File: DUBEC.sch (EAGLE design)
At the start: 47 parts

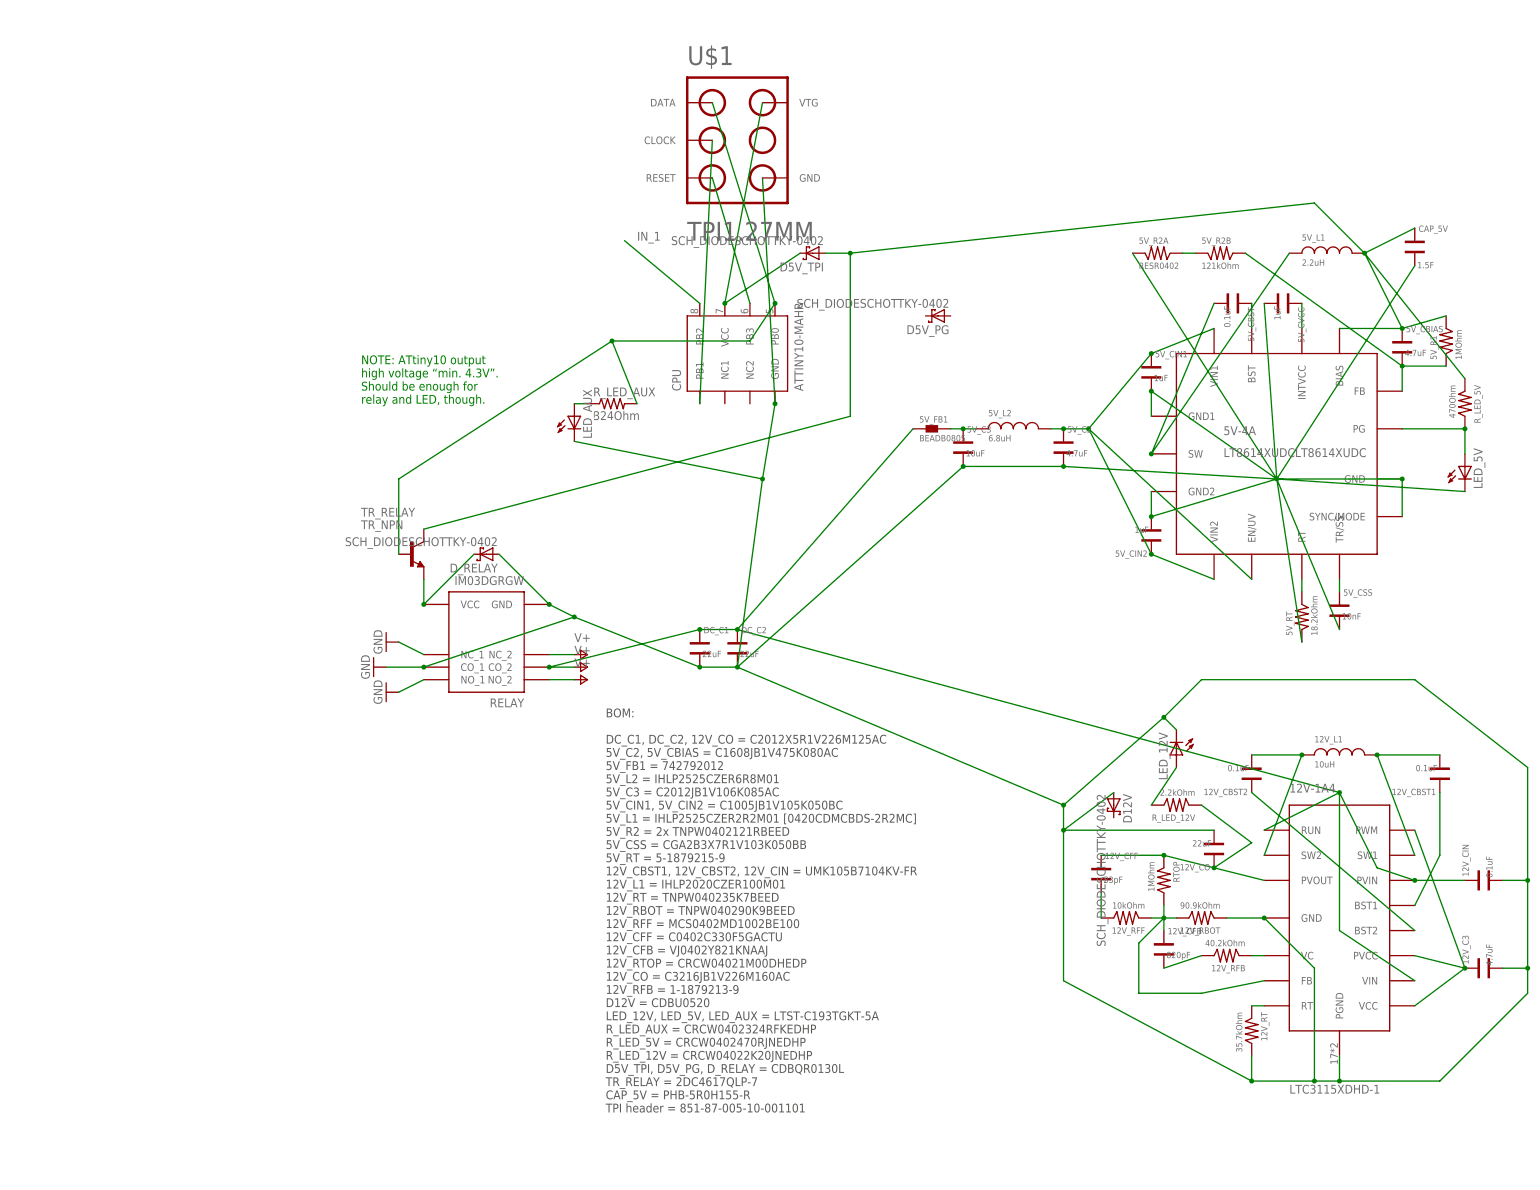
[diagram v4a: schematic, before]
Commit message: Switch to ATtiny13A (EEPROM)
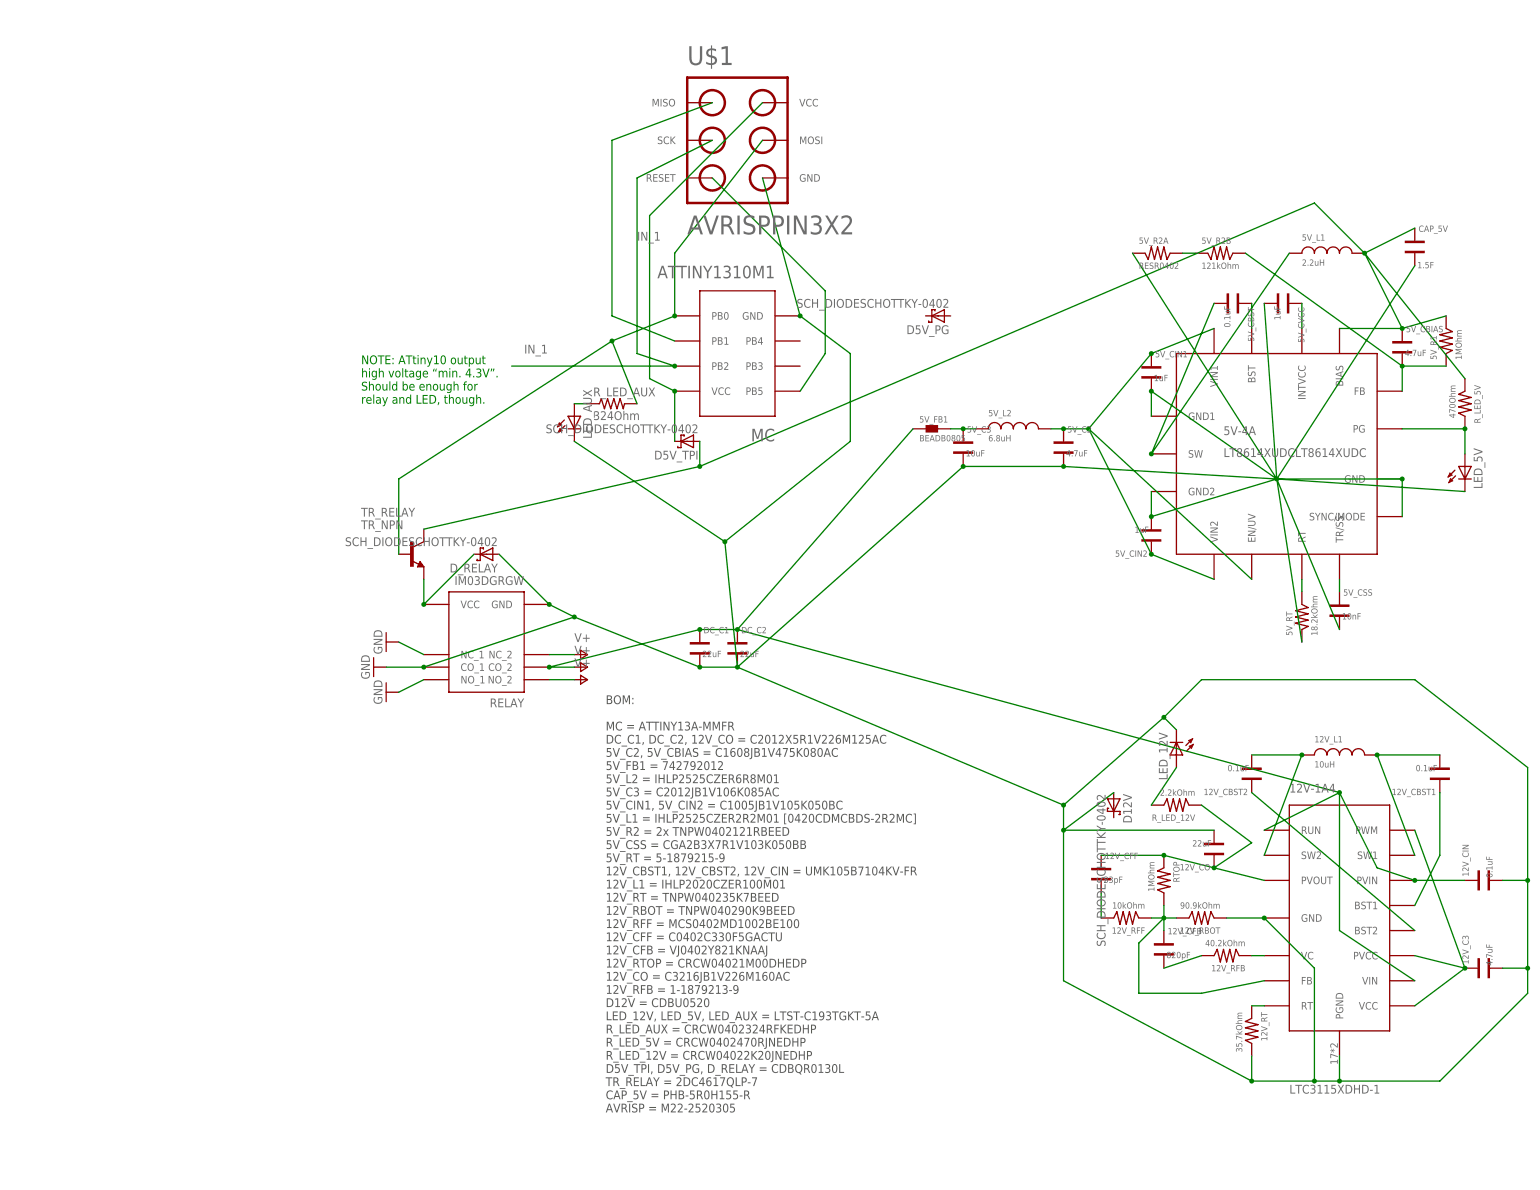
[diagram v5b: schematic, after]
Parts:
- removed CPU: ATTINY10-MAHR, jne:ATTINY10-MAHR
- added MC: ATTINY1310M1, dubec:ATTINY1310M1
- U$1: value TPI1.27MM -> AVRISPPIN3X2; device dubec:TPI1.27MM -> dubec:AVRISPPIN3X2
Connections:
- removed net 5V_TPI: CPU.VCC, D5V_TPI.C, U$1.VTG
- removed net PB1: CPU.PB1, U$1.CLOCK
- removed net PB3: CPU.PB3, U$1.RESET
- new net 5V_ISP: D5V_TPI.C, MC.VCC, U$1.VCC
- new net N$11: MC.PB5, U$1.RESET
- new net N$16: MC.PB1, U$1.MISO
- net GND: now also MC.GND; no longer CPU.GND
- net IN_1: now also MC.PB2, U$1.SCK; no longer CPU.PB2
- net PB0: now also MC.PB0, U$1.MOSI; no longer CPU.PB0, U$1.DATA
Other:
- note added: "BOM: MC = ATTINY13A-MMFR DC_C1, DC_C2, 12V_CO = C2012X5R1V226M125AC 5V_C2, 5V_CBIAS = C1608JB1V475K080AC 5V_FB1 = 742792012 5V_L2 = IHLP2525CZER6R8M01 5V_C3 = C2012JB1V106K085AC 5V_CIN1, 5V_CIN2 = C1005JB1V105K050BC 5V_L1 = IHLP2525CZER2R2M01 [0420CDMCBDS-2R2MC] 5V_R2 = 2x TNPW0402121RBEED 5V_CSS = CGA2B3X7R1V103K050BB 5V_RT = 5-1879215-9 12V_CBST1, 12V_CBST2, 12V_CIN = UMK105B7104KV-FR 12V_L1 = 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"
- note removed: "BOM: DC_C1, DC_C2, 12V_CO = C2012X5R1V226M125AC 5V_C2, 5V_CBIAS = C1608JB1V475K080AC 5V_FB1 = 742792012 5V_L2 = IHLP2525CZER6R8M01 5V_C3 = C2012JB1V106K085AC 5V_CIN1, 5V_CIN2 = C1005JB1V105K050BC 5V_L1 = IHLP2525CZER2R2M01 [0420CDMCBDS-2R2MC] 5V_R2 = 2x TNPW0402121RBEED 5V_CSS = CGA2B3X7R1V103K050BB 5V_RT = 5-1879215-9 12V_CBST1, 12V_CBST2, 12V_CIN = UMK105B7104KV-FR 12V_L1 = IHLP2020CZER100M01 1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"
- moved on the sheet: D5V_TPI
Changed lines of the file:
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@@
 <parts>
 <part name="5V-4A" library="jne" deviceset="LT8614XUDC" device="LT8614XUDC"/>
-<part name="CPU" library="jne" deviceset="ATTINY10-MAHR" device=""/>
+<part name="MC" library="dubec" deviceset="ATTINY13" device="10M1"/>
 <part name="RELAY" library="jne" deviceset="IM03DGR" device="GW"/>
 <part name="12V-1A4" library="jne" deviceset="LTC3115XDHD-1" device=""/>
@@
 <part name="R_LED_12V" library="jne" deviceset="RES" device="R0402" value="2.2kOhm"/>
 <part name="R_LED_5V" library="jne" deviceset="RES" device="R0402" value="470Ohm"/>
-<part name="U$1" library="dubec" deviceset="TPI" device="1.27MM" value="TPI1.27MM"/>
+<part name="U$1" library="dubec" deviceset="AVRISP" device="PIN3X2" value="AVRISPPIN3X2"/>
 <part name="D5V_PG" library="dubec" deviceset="SCH_DIODE" device="SCHOTTKY-0402"/>
 <part name="D5V_TPI" library="dubec" deviceset="SCH_DIODE" device="SCHOTTKY-0402"/>
@@
 <plain>
 <text x="-67.31" y="-107.95" size="1.778" layer="97">BOM:
+MC = ATTINY13A-MMFR
 DC_C1, DC_C2, 12V_CO = C2012X5R1V226M125AC
 5V_C2, 5V_CBIAS = C1608JB1V475K080AC
@@
 TR_RELAY = 2DC4617QLP-7
 CAP_5V = PHB-5R0H155-R
-TPI header = 851-87-005-10-001101
+AVRISP = M22-2520305
 </text>
 <text x="-116.84" y="35.56" size="1.778" layer="91">NOTE: ATtiny10 output
@@
 <instances>
 <instance part="5V-4A" gate="G$1" x="68.58" y="25.4"/>
-<instance part="CPU" gate="G$1" x="-40.64" y="45.72" rot="R90"/>
+<instance part="MC" gate="G$1" x="-40.64" y="45.72" rot="R180"/>
 <instance part="RELAY" gate="G$1" x="-91.44" y="-12.7" rot="R180"/>
 <instance part="12V-1A4" gate="G$1" x="81.28" y="-68.58"/>
@@
 <instance part="U$1" gate="G$1" x="-40.64" y="88.9"/>
 <instance part="D5V_PG" gate="G$1" x="0" y="53.34" rot="R180"/>
-<instance part="D5V_TPI" gate="G$1" x="-25.4" y="66.04" rot="R180"/>
+<instance part="D5V_TPI" gate="G$1" x="-50.8" y="27.94" rot="R180"/>
 <instance part="TR_RELAY" gate="G$1" x="-106.68" y="5.08"/>
 <instance part="D_RELAY" gate="G$1" x="-91.44" y="5.08" rot="R180"/>
@@
 <wire x1="106.68" y1="40.64" x2="86.36" y2="66.04" width="0.1524" layer="91"/>
 <pinref part="D5V_TPI" gate="G$1" pin="A"/>
-<wire x1="-22.86" y1="66.04" x2="-17.78" y2="66.04" width="0.1524" layer="91"/>
-<wire x1="-17.78" y1="66.04" x2="76.2" y2="76.2" width="0.1524" layer="91"/>
+<wire x1="-48.26" y1="27.94" x2="-48.26" y2="22.86" width="0.1524" layer="91"/>
+<wire x1="-48.26" y1="22.86" x2="76.2" y2="76.2" width="0.1524" layer="91"/>
 <wire x1="76.2" y1="76.2" x2="86.36" y2="66.04" width="0.1524" layer="91"/>
-<wire x1="-17.78" y1="66.04" x2="-17.78" y2="33.02" width="0.1524" layer="91"/>
-<junction x="-17.78" y="66.04"/>
+<junction x="-48.26" y="22.86"/>
 <pinref part="TR_RELAY" gate="G$1" pin="C"/>
-<wire x1="-104.14" y1="10.16" x2="-17.78" y2="33.02" width="0.1524" layer="91"/>
+<wire x1="-104.14" y1="10.16" x2="-48.26" y2="22.86" width="0.1524" layer="91"/>
 <pinref part="CAP_5V" gate="G$1" pin="V+"/>
 <wire x1="86.36" y1="66.04" x2="96.52" y2="71.12" width="0.1524" layer="91"/>
@@
 <pinref part="12V_CIN" gate="G$1" pin="GND"/>
 <pinref part="12V_C3" gate="G$1" pin="GND"/>
-<pinref part="CPU" gate="G$1" pin="GND"/>
-<wire x1="-33.02" y1="35.56" x2="-35.56" y2="20.32" width="0.1524" layer="91"/>
-<wire x1="-35.56" y1="20.32" x2="-40.64" y2="-17.78" width="0.1524" layer="91"/>
+<pinref part="MC" gate="G$1" pin="GND"/>
+<wire x1="-27.94" y1="53.34" x2="-17.78" y2="45.72" width="0.1524" layer="91"/>
+<wire x1="-17.78" y1="45.72" x2="-17.78" y2="27.94" width="0.1524" layer="91"/>
+<wire x1="-17.78" y1="27.94" x2="-43.18" y2="7.62" width="0.1524" layer="91"/>
+<wire x1="-43.18" y1="7.62" x2="-40.64" y2="-17.78" width="0.1524" layer="91"/>
 <junction x="-104.14" y="-17.78"/>
 <junction x="-78.74" y="-5.08"/>
@@
 <wire x1="106.68" y1="17.78" x2="68.58" y2="20.32" width="0.1524" layer="91"/>
 <pinref part="LED_AUX" gate="G$1" pin="C"/>
-<junction x="-33.02" y="35.56"/>
-<pinref part="U$1" gate="G$1" pin="GND"/>
-<wire x1="-33.02" y1="35.56" x2="-35.56" y2="81.28" width="0.1524" layer="91"/>
 <pinref part="D_RELAY" gate="G$1" pin="A"/>
 <wire x1="-78.74" y1="-5.08" x2="-88.9" y2="5.08" width="0.1524" layer="91"/>
@@
 <wire x1="76.2" y1="-78.74" x2="76.2" y2="-101.6" width="0.1524" layer="91"/>
 <junction x="76.2" y="-101.6"/>
-<wire x1="-73.66" y1="27.94" x2="-35.56" y2="20.32" width="0.1524" layer="91"/>
-<junction x="-35.56" y="20.32"/>
+<wire x1="-73.66" y1="27.94" x2="-43.18" y2="7.62" width="0.1524" layer="91"/>
+<junction x="-43.18" y="7.62"/>
 <pinref part="D12V" gate="G$1" pin="A"/>
 <wire x1="25.4" y1="-50.8" x2="35.56" y2="-43.18" width="0.1524" layer="91"/>
+<pinref part="U$1" gate="G$1" pin="GND"/>
+<wire x1="-27.94" y1="53.34" x2="-35.56" y2="81.28" width="0.1524" layer="91"/>
+<junction x="-27.94" y="53.34"/>
 </segment>
 </net>
@@
 </segment>
 </net>
-<net name="PB1" class="0">
-<segment>
-<pinref part="CPU" gate="G$1" pin="PB1"/>
-<pinref part="U$1" gate="G$1" pin="CLOCK"/>
-<wire x1="-48.26" y1="35.56" x2="-45.72" y2="88.9" width="0.1524" layer="91"/>
-</segment>
-</net>
 <net name="PB0" class="0">
 <segment>
-<pinref part="CPU" gate="G$1" pin="PB0"/>
-<pinref part="U$1" gate="G$1" pin="DATA"/>
-<wire x1="-33.02" y1="55.88" x2="-45.72" y2="96.52" width="0.1524" layer="91"/>
-<junction x="-33.02" y="55.88"/>
+<pinref part="MC" gate="G$1" pin="PB0"/>
 <pinref part="R_LED_AUX" gate="G$1" pin="2"/>
 <wire x1="-60.96" y1="35.56" x2="-66.04" y2="48.26" width="0.1524" layer="91"/>
-<wire x1="-66.04" y1="48.26" x2="-38.1" y2="48.26" width="0.1524" layer="91"/>
-<wire x1="-38.1" y1="48.26" x2="-33.02" y2="55.88" width="0.1524" layer="91"/>
+<wire x1="-66.04" y1="48.26" x2="-53.34" y2="53.34" width="0.1524" layer="91"/>
 <pinref part="TR_RELAY" gate="G$1" pin="B"/>
 <wire x1="-109.22" y1="5.08" x2="-109.22" y2="20.32" width="0.1524" layer="91"/>
 <wire x1="-109.22" y1="20.32" x2="-66.04" y2="48.26" width="0.1524" layer="91"/>
 <junction x="-66.04" y="48.26"/>
+<pinref part="U$1" gate="G$1" pin="MOSI"/>
+<wire x1="-53.34" y1="53.34" x2="-53.34" y2="66.04" width="0.1524" layer="91"/>
+<wire x1="-53.34" y1="66.04" x2="-35.56" y2="88.9" width="0.1524" layer="91"/>
+<junction x="-53.34" y="53.34"/>
 </segment>
 </net>
 <net name="IN_1" class="0">
 <segment>
-<pinref part="CPU" gate="G$1" pin="PB2"/>
-<wire x1="-48.26" y1="55.88" x2="-63.5" y2="68.58" width="0.1524" layer="91"/>
+<pinref part="MC" gate="G$1" pin="PB2"/>
+<wire x1="-53.34" y1="43.18" x2="-86.36" y2="43.18" width="0.1524" layer="91"/>
 <label x="-60.96" y="68.58" size="1.778" layer="95"/>
-</segment>
-</net>
-<net name="5V_TPI" class="0">
+<pinref part="U$1" gate="G$1" pin="SCK"/>
+<wire x1="-53.34" y1="43.18" x2="-60.96" y2="45.72" width="0.1524" layer="91"/>
+<wire x1="-60.96" y1="45.72" x2="-60.96" y2="81.28" width="0.1524" layer="91"/>
+<wire x1="-60.96" y1="81.28" x2="-45.72" y2="88.9" width="0.1524" layer="91"/>
+<junction x="-53.34" y="43.18"/>
+<label x="-83.82" y="45.72" size="1.778" layer="95"/>
+</segment>
+</net>
+<net name="5V_ISP" class="0">
 <segment>
 <pinref part="D5V_TPI" gate="G$1" pin="C"/>
-<pinref part="U$1" gate="G$1" pin="VTG"/>
-<pinref part="CPU" gate="G$1" pin="VCC"/>
-<wire x1="-43.18" y1="55.88" x2="-35.56" y2="96.52" width="0.1524" layer="91"/>
-<wire x1="-27.94" y1="66.04" x2="-43.18" y2="55.88" width="0.1524" layer="91"/>
-<junction x="-43.18" y="55.88"/>
+<pinref part="MC" gate="G$1" pin="VCC"/>
+<wire x1="-53.34" y1="27.94" x2="-53.34" y2="38.1" width="0.1524" layer="91"/>
+<pinref part="U$1" gate="G$1" pin="VCC"/>
+<wire x1="-53.34" y1="38.1" x2="-58.42" y2="40.64" width="0.1524" layer="91"/>
+<wire x1="-58.42" y1="40.64" x2="-58.42" y2="73.66" width="0.1524" layer="91"/>
+<wire x1="-58.42" y1="73.66" x2="-35.56" y2="96.52" width="0.1524" layer="91"/>
+<junction x="-53.34" y="38.1"/>
 </segment>
 </net>
@@
 </segment>
 </net>
-<net name="PB3" class="0">
-<segment>
+<net name="N$11" class="0">
+<segment>
+<pinref part="MC" gate="G$1" pin="PB5"/>
 <pinref part="U$1" gate="G$1" pin="RESET"/>
-<pinref part="CPU" gate="G$1" pin="PB3"/>
-<wire x1="-45.72" y1="81.28" x2="-38.1" y2="55.88" width="0.1524" layer="91"/>
-</segment>
-</net>
+<wire x1="-27.94" y1="38.1" x2="-22.86" y2="45.72" width="0.1524" layer="91"/>
+<wire x1="-22.86" y1="45.72" x2="-22.86" y2="58.42" width="0.1524" layer="91"/>
+<wire x1="-22.86" y1="58.42" x2="-45.72" y2="81.28" width="0.1524" layer="91"/>
+</segment>
+</net>
+<net name="N$16" class="0">
+<segment>
+<pinref part="MC" gate="G$1" pin="PB1"/>
+<pinref part="U$1" gate="G$1" pin="MISO"/>
+<wire x1="-53.34" y1="48.26" x2="-66.04" y2="53.34" width="0.1524" layer="91"/>
+<wire x1="-66.04" y1="53.34" x2="-66.04" y2="88.9" width="0.1524" layer="91"/>
+<wire x1="-66.04" y1="88.9" x2="-45.72" y2="96.52" width="0.1524" layer="91"/>
+</segment>
+</net>

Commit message: Voltage divider
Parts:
- removed D5V_PG, D5V_TPI: SCH_DIODESCHOTTKY-0402, dubec:SCH_DIODESCHOTTKY-0402
- added D5V_ISP: SCH_DIODESCHOTTKY-0402, dubec:SCH_DIODESCHOTTKY-0402
- added R_DIV_1: 15kOhm, dubec:RESR0402
- added R_DIV_2: 2.5kOhm, dubec:RESR0402
- added ZD_DIV: 5.1V, dubec:Z-DIODE
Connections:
- net N$11 renamed PB5
- net N$16 renamed MISO
- net PB0 renamed RELAY_CONTROL
- new net N$17: MC.PB3, R_DIV_1.GND, R_DIV_2.GND, ZD_DIV.A
- net 35V: now also R_DIV_1.1
- net 5V: now also D5V_ISP.A; no longer D5V_TPI.A
- net 5V_ISP: now also D5V_ISP.C; no longer D5V_TPI.C
- net GND: now also R_DIV_2.1, ZD_DIV.C
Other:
- moved on the sheet: LED_AUX, R_LED_AUX

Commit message: Cleaning up
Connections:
- new net 5V_RAW: 5V-4A.SW, 5V_CBST.GND, 5V_L1.1
- net 12V: now also D12V.C
- net 5V: no longer 5V-4A.SW, 5V_CBST.GND, 5V_L1.1
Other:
- moved on the sheet: D12V, R_LED_12V
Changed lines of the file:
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@@
 <setting verticaltext="up"/>
 </settings>
-<grid distance="0.05" unitdist="inch" unit="inch" style="lines" multiple="10" display="no" altdistance="0.01" altunitdist="inch" altunit="inch"/>
+<grid distance="0.1" unitdist="inch" unit="inch" style="lines" multiple="1" display="no" altdistance="0.01" altunitdist="inch" altunit="inch"/>
 <layers>
 <layer number="1" name="Top" color="4" fill="1" visible="no" active="no"/>
@@
 <instance part="LED_AUX" gate="G$1" x="-67.31" y="29.21"/>
 <instance part="R_LED_AUX" gate="G$1" x="-67.31" y="40.64" rot="R90"/>
-<instance part="R_LED_12V" gate="G$1" x="48.26" y="-45.72" rot="R180"/>
+<instance part="R_LED_12V" gate="G$1" x="53.34" y="-45.72" rot="R180"/>
 <instance part="R_LED_5V" gate="G$1" x="106.68" y="35.56" rot="R270"/>
 <instance part="U$1" gate="G$1" x="-40.64" y="88.9"/>
@@
 <instance part="D_RELAY" gate="G$1" x="-91.44" y="5.08" rot="R180"/>
 <instance part="CAP_5V" gate="G$1" x="96.52" y="68.58"/>
-<instance part="D12V" gate="G$1" x="35.56" y="-45.72" rot="R270"/>
+<instance part="D12V" gate="G$1" x="35.56" y="-48.26"/>
 <instance part="R_DIV_1" gate="G$1" x="-54.61" y="0"/>
 <instance part="R_DIV_2" gate="G$1" x="-54.61" y="8.89"/>
@@
 <net name="5V" class="0">
 <segment>
-<pinref part="5V-4A" gate="G$1" pin="SW"/>
-<pinref part="5V_L1" gate="G$1" pin="1"/>
-<wire x1="43.18" y1="25.4" x2="71.12" y2="35.56" width="0.1524" layer="91"/>
-<wire x1="71.12" y1="35.56" x2="71.12" y2="66.04" width="0.1524" layer="91"/>
-<pinref part="5V_CBST" gate="G$1" pin="GND"/>
-<wire x1="55.88" y1="55.88" x2="43.18" y2="25.4" width="0.1524" layer="91"/>
-<junction x="43.18" y="25.4"/>
-</segment>
-<segment>
 <pinref part="5V_CBIAS" gate="G$1" pin="V+"/>
 <pinref part="5V-4A" gate="G$1" pin="BIAS"/>
@@
 <junction x="45.72" y="-55.88"/>
 <pinref part="R_LED_12V" gate="G$1" pin="1"/>
-<wire x1="53.34" y1="-45.72" x2="63.5" y2="-53.34" width="0.1524" layer="91"/>
-<wire x1="63.5" y1="-53.34" x2="55.88" y2="-58.42" width="0.1524" layer="91"/>
+<wire x1="58.42" y1="-45.72" x2="63.5" y2="-50.8" width="0.1524" layer="91"/>
+<wire x1="63.5" y1="-50.8" x2="55.88" y2="-58.42" width="0.1524" layer="91"/>
+<pinref part="D12V" gate="G$1" pin="C"/>
+<wire x1="38.1" y1="-48.26" x2="55.88" y2="-48.26" width="0.1524" layer="91"/>
+<wire x1="55.88" y1="-48.26" x2="66.04" y2="-60.96" width="0.1524" layer="91"/>
+<junction x="66.04" y="-60.96"/>
 </segment>
 </net>
@@
 <junction x="-39.37" y="12.7"/>
 <pinref part="D12V" gate="G$1" pin="A"/>
-<wire x1="25.4" y1="-50.8" x2="35.56" y2="-43.18" width="0.1524" layer="91"/>
+<wire x1="25.4" y1="-50.8" x2="33.02" y2="-48.26" width="0.1524" layer="91"/>
 <pinref part="U$1" gate="G$1" pin="GND"/>
 <wire x1="-27.94" y1="53.34" x2="-35.56" y2="81.28" width="0.1524" layer="91"/>
@@
 <pinref part="R_LED_12V" gate="G$1" pin="GND"/>
 <pinref part="LED_12V" gate="G$1" pin="A"/>
-<wire x1="43.18" y1="-45.72" x2="48.26" y2="-38.1" width="0.1524" layer="91"/>
+<wire x1="48.26" y1="-45.72" x2="48.26" y2="-38.1" width="0.1524" layer="91"/>
 </segment>
 </net>
@@
 </segment>
 </net>
+<net name="5V_RAW" class="0">
+<segment>
+<pinref part="5V_CBST" gate="G$1" pin="GND"/>
+<wire x1="55.88" y1="55.88" x2="50.8" y2="50.8" width="0.1524" layer="91"/>
+<wire x1="50.8" y1="50.8" x2="50.8" y2="33.02" width="0.1524" layer="91"/>
+<pinref part="5V-4A" gate="G$1" pin="SW"/>
+<wire x1="50.8" y1="33.02" x2="43.18" y2="25.4" width="0.1524" layer="91"/>
+<wire x1="43.18" y1="25.4" x2="58.42" y2="25.4" width="0.1524" layer="91"/>
+<wire x1="58.42" y1="25.4" x2="71.12" y2="38.1" width="0.1524" layer="91"/>
+<junction x="43.18" y="25.4"/>
+<pinref part="5V_L1" gate="G$1" pin="1"/>
+<wire x1="71.12" y1="38.1" x2="71.12" y2="66.04" width="0.1524" layer="91"/>
+</segment>
+</net>
